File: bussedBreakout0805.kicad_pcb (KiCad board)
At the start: 2 copper layers, 2.9 x 2.9 mm, 46 parts, among them J1 Conn_01x12_Pin, J10 Conn_01x06_Pin, J11 Conn_01x06_Pin, J12 Conn_01x06_Pin, J13 Conn_01x06_Pin, J14 Conn_01x06_Pin, J15 Conn_01x06_Pin, J16 Conn_01x06_Pin, J17 Conn_01x06_Pin, J18 Conn_01x06_Pin, J19 Conn_01x06_Pin, J2 Conn_01x01_Pin, J20 Conn_01x06_Pin, J21 Conn_01x06_Pin, J22 Conn_01x06_Pin, J23 Conn_01x06_Pin, J24 Conn_01x06_Pin, J25 Conn_01x06_Pin, J26 Conn_01x06_Pin, J27 Conn_01x06_Pin, J28 Conn_01x06_Pin, J29 Conn_01x06_Pin, J3 Conn_01x01_Pin, J30 Conn_01x06_Pin, J31 Conn_01x06_Pin, J32 Conn_01x06_Pin, J4 Conn_01x05_Pin, J5 Conn_01x05_Pin, J6 Conn_01x01_Pin, J7 Conn_01x01_Pin, J8 Conn_01x12_Pin, J9 Conn_01x06_Pin

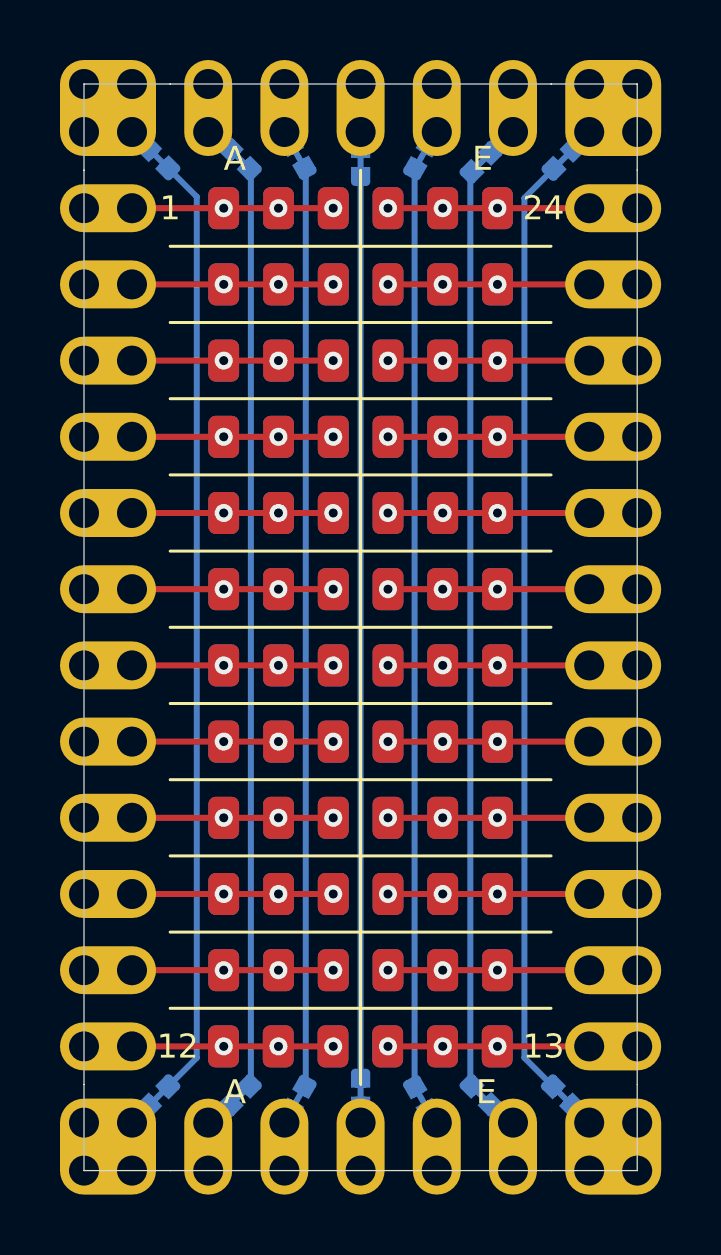
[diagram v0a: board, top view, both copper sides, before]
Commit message: Add VCC/GND buses on opposite sides, add V[CC]/G[ND] labels, move labels away from solder mask cutouts
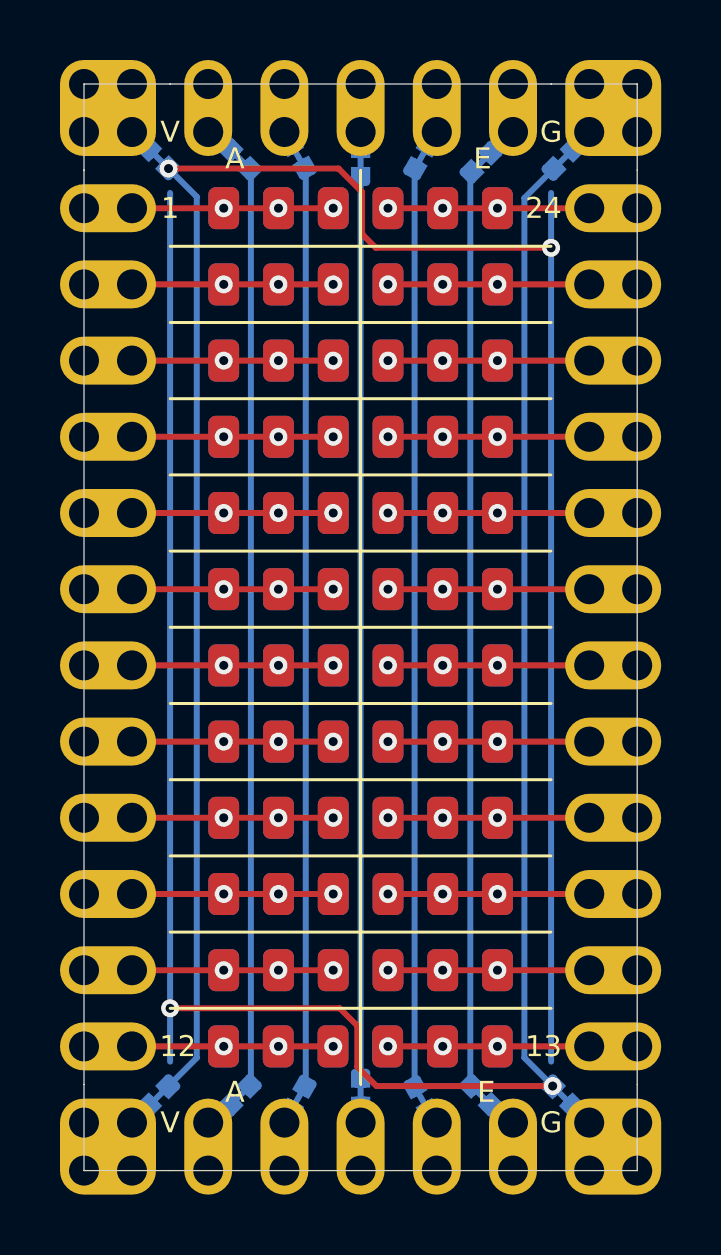
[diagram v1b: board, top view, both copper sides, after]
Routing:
- net VCC: track 31.4 -> 75.0 mm, vias 0 -> 2
- net GND: track 31.4 -> 74.9 mm, vias 0 -> 2
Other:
- board text added: "G"
- board text added: "V"
